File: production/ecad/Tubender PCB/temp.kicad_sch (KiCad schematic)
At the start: 5 parts, among them IC5 SN74HC138PWR, IC6 SN74HC138PWR, IC7 SN74LVC1G29DCTR, U7 74HC595

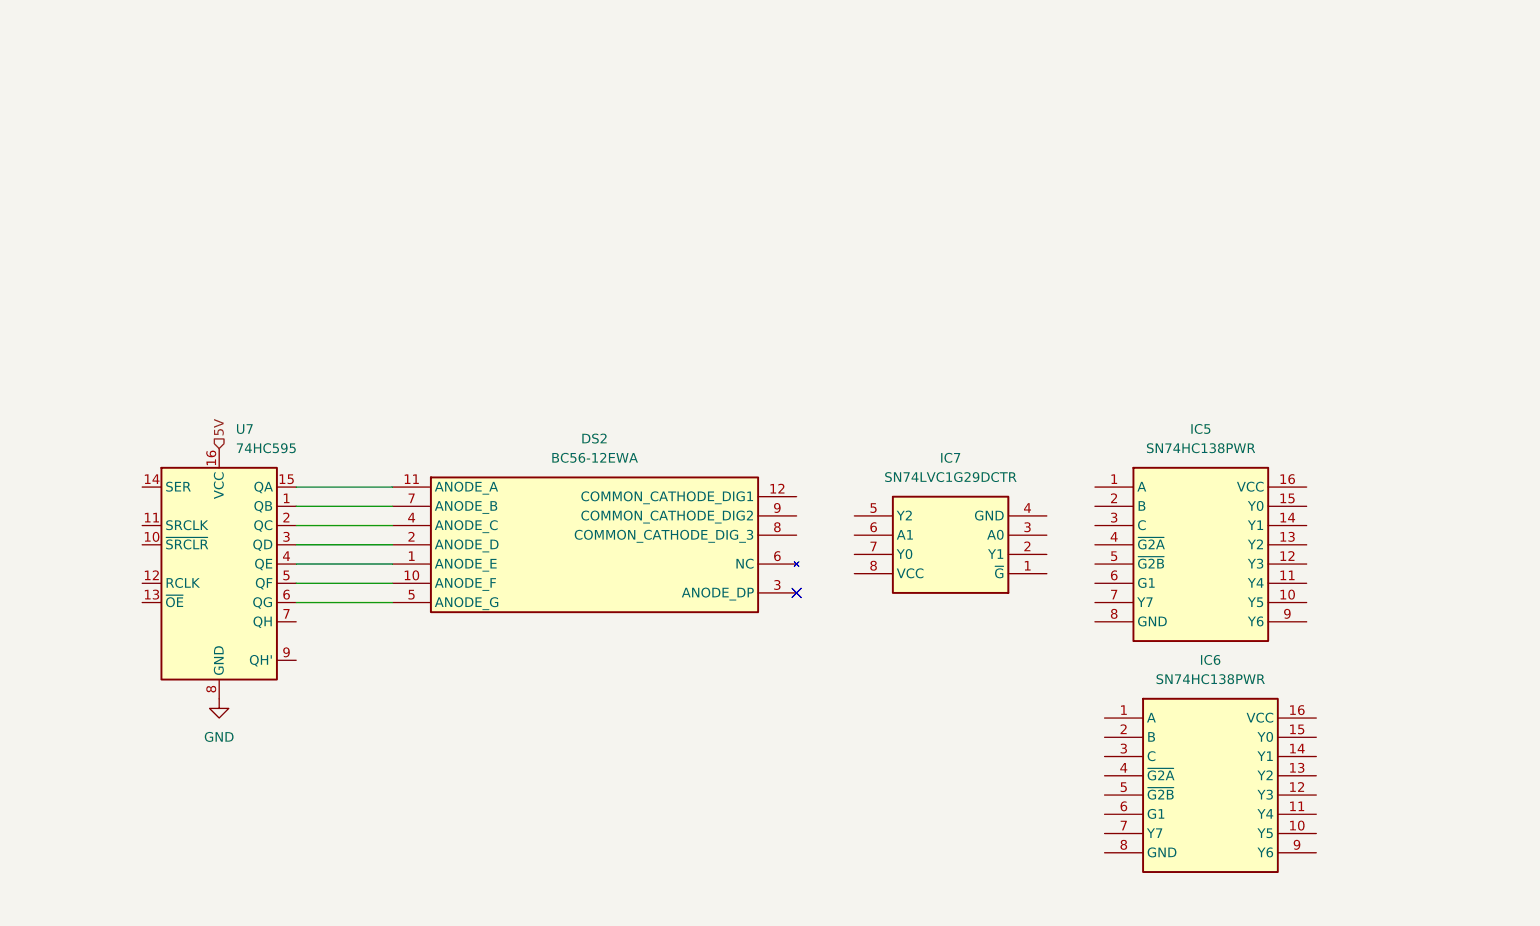
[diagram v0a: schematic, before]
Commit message: 7 Segment, Buttons, Plexers Oh MY!
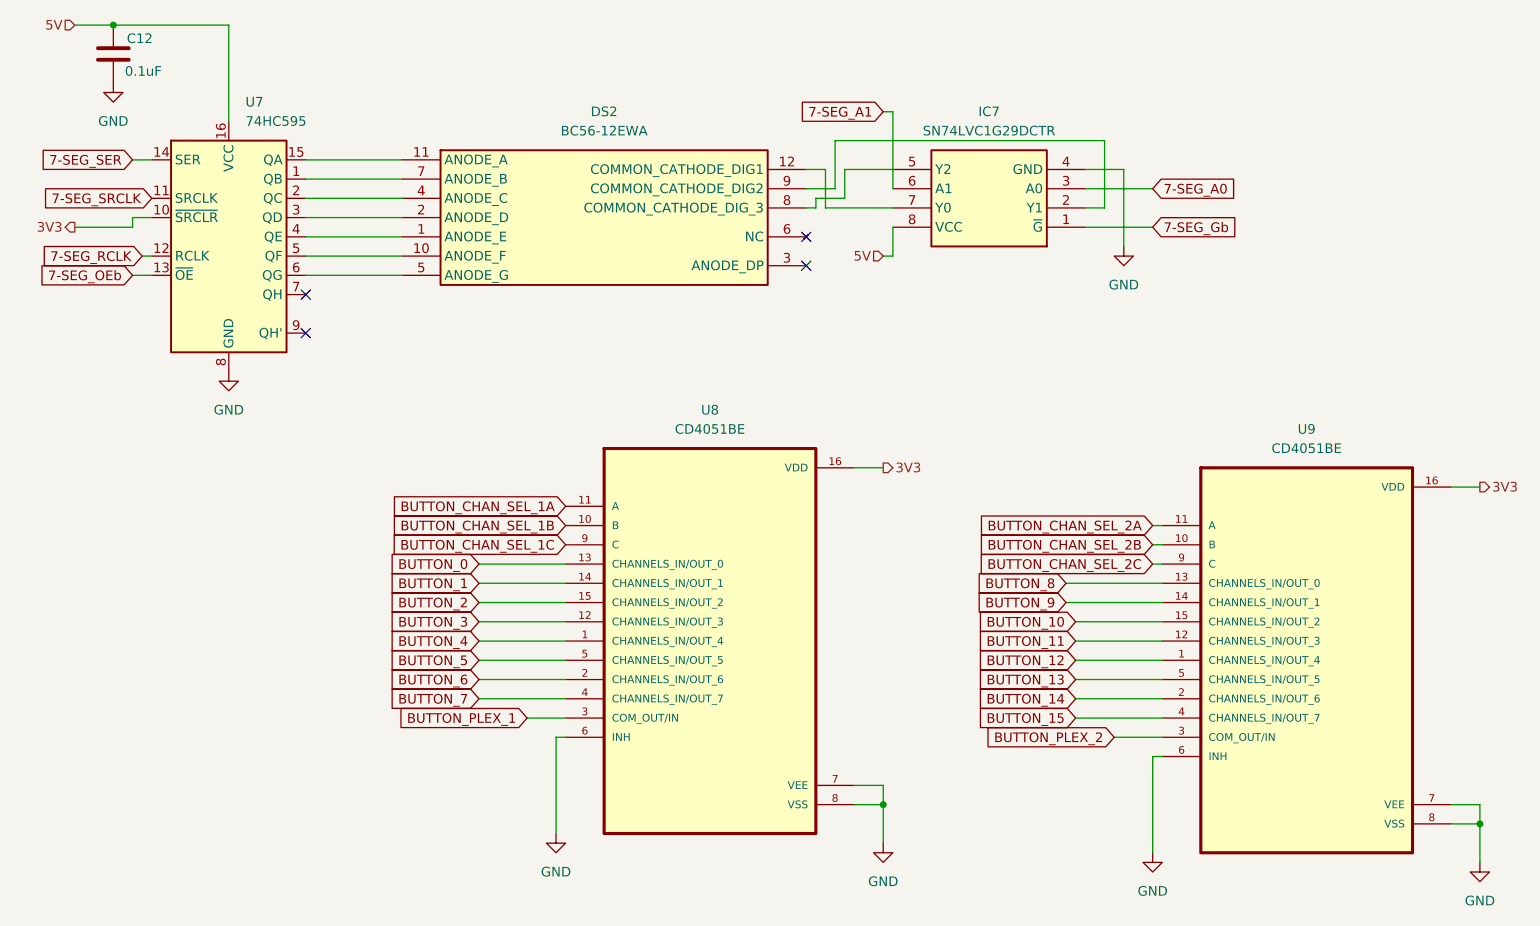
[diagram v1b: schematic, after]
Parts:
- removed IC5, IC6: SN74HC138PWR, SOP65P640X120-16N, symbol SamacSys_Parts:SN74HC138PWR
- added C12: 0.1uF, symbol Device:C
- added U8, U9: CD4051BE, CD4051BE:DIP794W45P254L1969H508Q16, symbol CD4051BE:CD4051BE
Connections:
- net 5V: now also IC7.8 (VCC), C12.1
- net GND: now also IC7.4 (GND), C12.2, U8.6 (INH), U8.7 (VEE), U8.8 (VSS), U9.6 (INH), U9.7 (VEE), U9.8 (VSS)
- net 7-SEG_Gb: now reaches IC7.1 (~{G})
- net at IC7.2 (Y1): now also DS2.9 (COMMON_CATHODE_DIG2)
- net 7-SEG_A0: now reaches IC7.3 (A0)
- net at IC7.5 (Y2): now also DS2.8 (COMMON_CATHODE_DIG_3)
- net 7-SEG_A1: now reaches IC7.6 (A1)
- net at IC7.7 (Y0): now also DS2.12 (COMMON_CATHODE_DIG1)
- net 3V3: now reaches U7.10 (~{SRCLR})
- net 3V3: now also U8.16 (VDD), U9.16 (VDD)
- net 7-SEG_SRCLK: now reaches U7.11 (SRCLK)
- net 7-SEG_RCLK: now reaches U7.12 (RCLK)
- net 7-SEG_OEb: now reaches U7.13 (~{OE})
- net 7-SEG_SER: now reaches U7.14 (SER)
- new net BUTTON_0: U8.13 (CHANNELS_IN/OUT_0)
- new net BUTTON_1: U8.14 (CHANNELS_IN/OUT_1)
- new net BUTTON_10: U9.15 (CHANNELS_IN/OUT_2)
- new net BUTTON_11: U9.12 (CHANNELS_IN/OUT_3)
- new net BUTTON_12: U9.1 (CHANNELS_IN/OUT_4)
- new net BUTTON_13: U9.5 (CHANNELS_IN/OUT_5)
- new net BUTTON_14: U9.2 (CHANNELS_IN/OUT_6)
- new net BUTTON_15: U9.4 (CHANNELS_IN/OUT_7)
- new net BUTTON_2: U8.15 (CHANNELS_IN/OUT_2)
- new net BUTTON_3: U8.12 (CHANNELS_IN/OUT_3)
- new net BUTTON_4: U8.1 (CHANNELS_IN/OUT_4)
- new net BUTTON_5: U8.5 (CHANNELS_IN/OUT_5)
- new net BUTTON_6: U8.2 (CHANNELS_IN/OUT_6)
- new net BUTTON_7: U8.4 (CHANNELS_IN/OUT_7)
- new net BUTTON_8: U9.13 (CHANNELS_IN/OUT_0)
- new net BUTTON_9: U9.14 (CHANNELS_IN/OUT_1)
- new net BUTTON_CHAN_SEL_1A: U8.11 (A)
- new net BUTTON_CHAN_SEL_1B: U8.10 (B)
- new net BUTTON_CHAN_SEL_1C: U8.9 (C)
- new net BUTTON_CHAN_SEL_2A: U9.11 (A)
- new net BUTTON_CHAN_SEL_2B: U9.10 (B)
- new net BUTTON_CHAN_SEL_2C: U9.9 (C)
- new net BUTTON_PLEX_1: U8.3 (COM_OUT/IN)
- new net BUTTON_PLEX_2: U9.3 (COM_OUT/IN)
- no-connect marks 1 -> 4
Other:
- moved on the sheet: DS2, IC7, U7
